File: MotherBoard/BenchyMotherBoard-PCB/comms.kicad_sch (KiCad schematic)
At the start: 9 parts, among them J18 COMMS-PWR, J19 COMMS-ELOAD, J20 COMMS-SWITCHER, J21 RELAYS-CONN, J22 COMMS-LOGIC

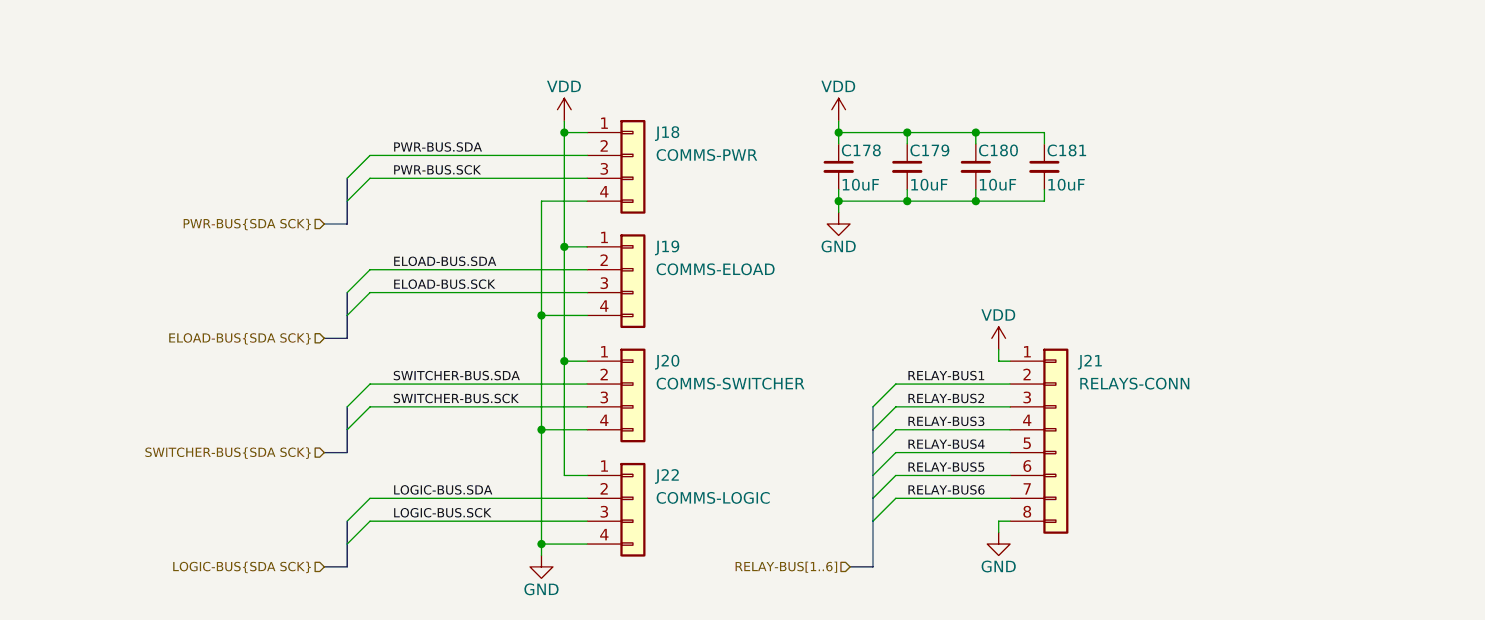
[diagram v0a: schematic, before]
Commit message: Add volt meter PCB
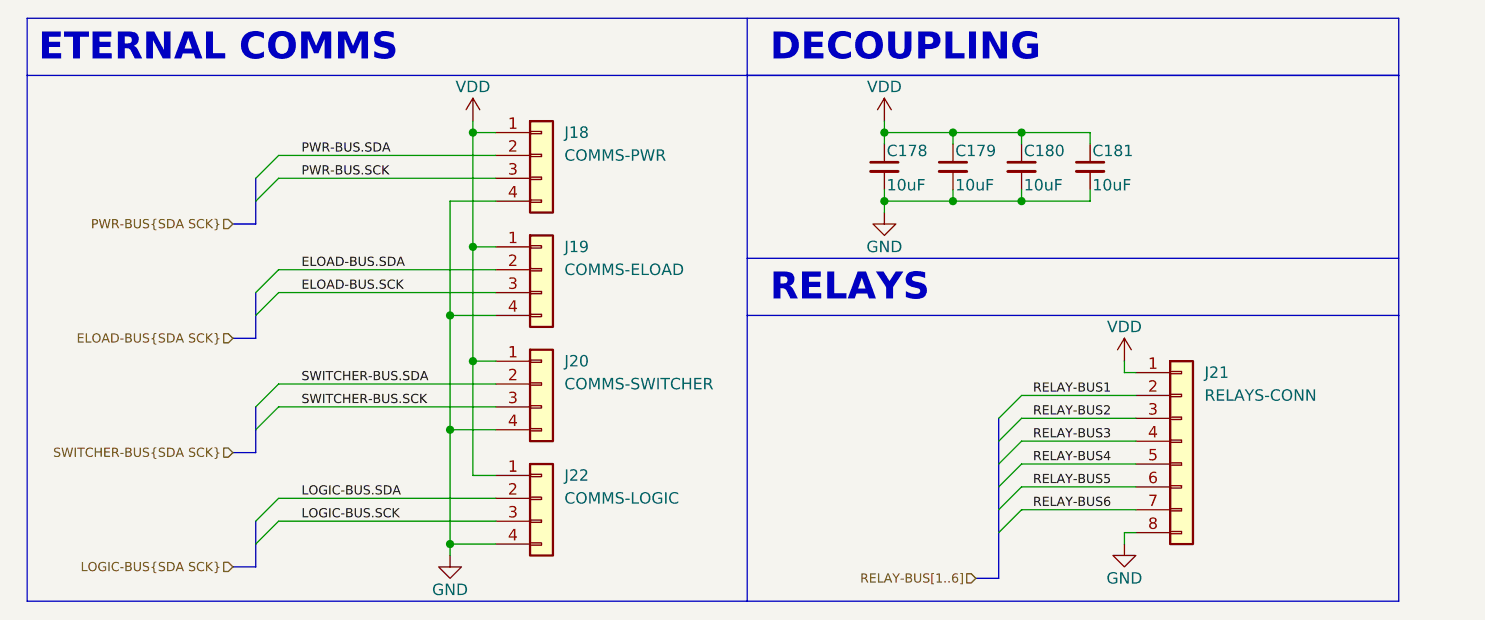
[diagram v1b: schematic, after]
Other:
- note added: "DECOUPLING"
- note added: "ETERNAL COMMS"
- note added: "RELAYS"
- moved on the sheet: C178, C179, C180, C181, J18, J19, J20, J21, J22

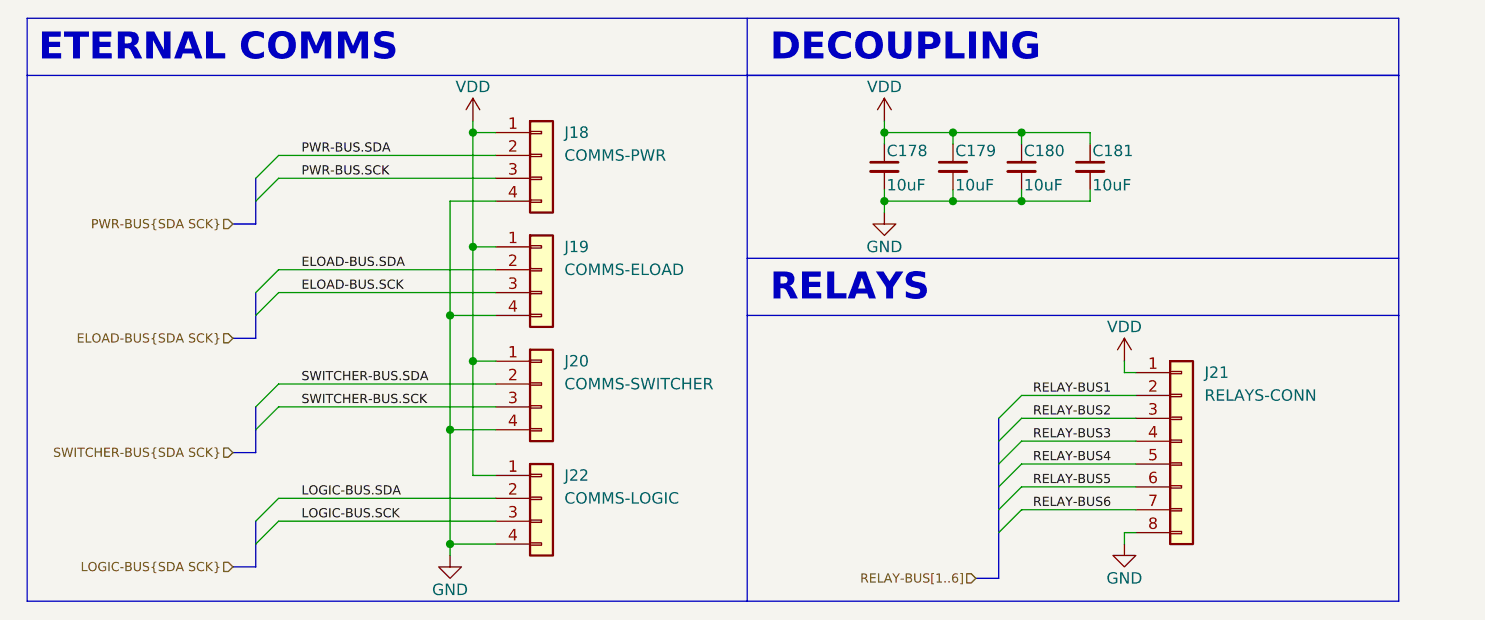
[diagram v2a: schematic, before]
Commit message: Finish trace layout and update PS fb resistor values
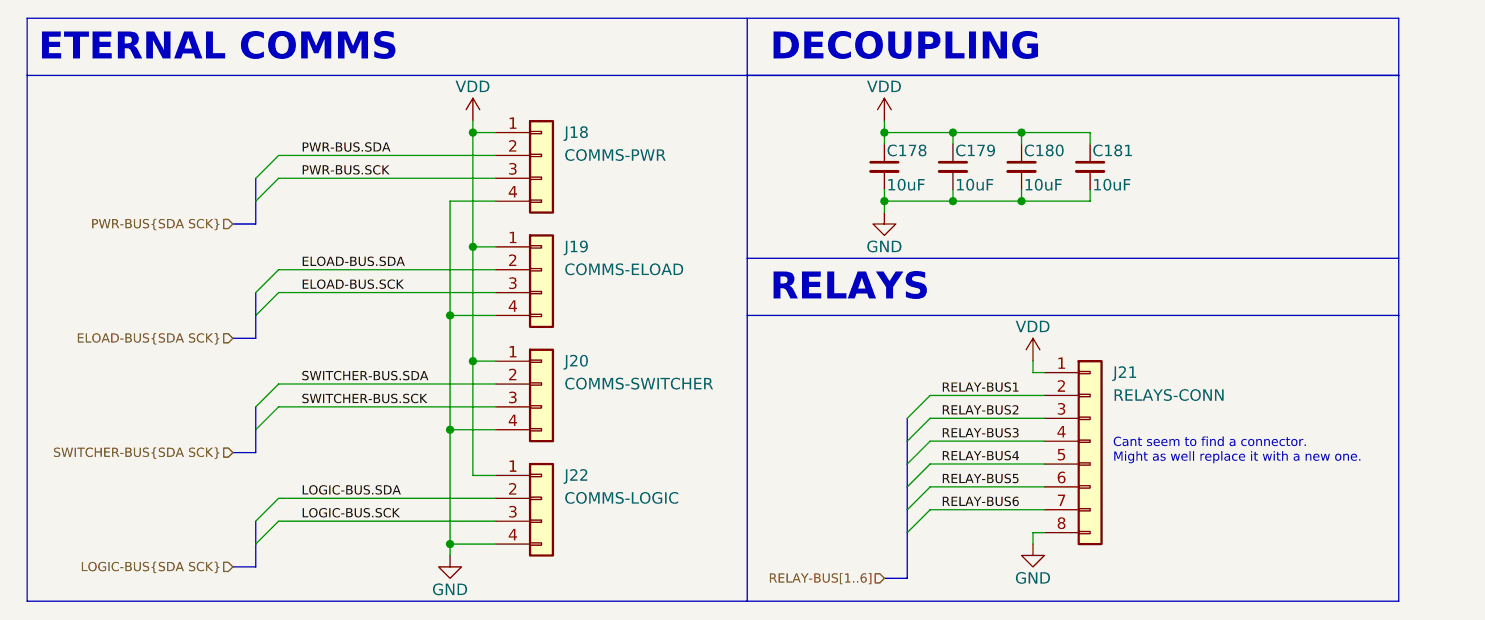
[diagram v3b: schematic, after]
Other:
- note added: "Cant seem to find a connector. Might as well replace it with a new one."
- moved on the sheet: J21
